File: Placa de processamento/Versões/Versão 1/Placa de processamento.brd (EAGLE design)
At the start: 90.2 x 100 mm, 12 parts

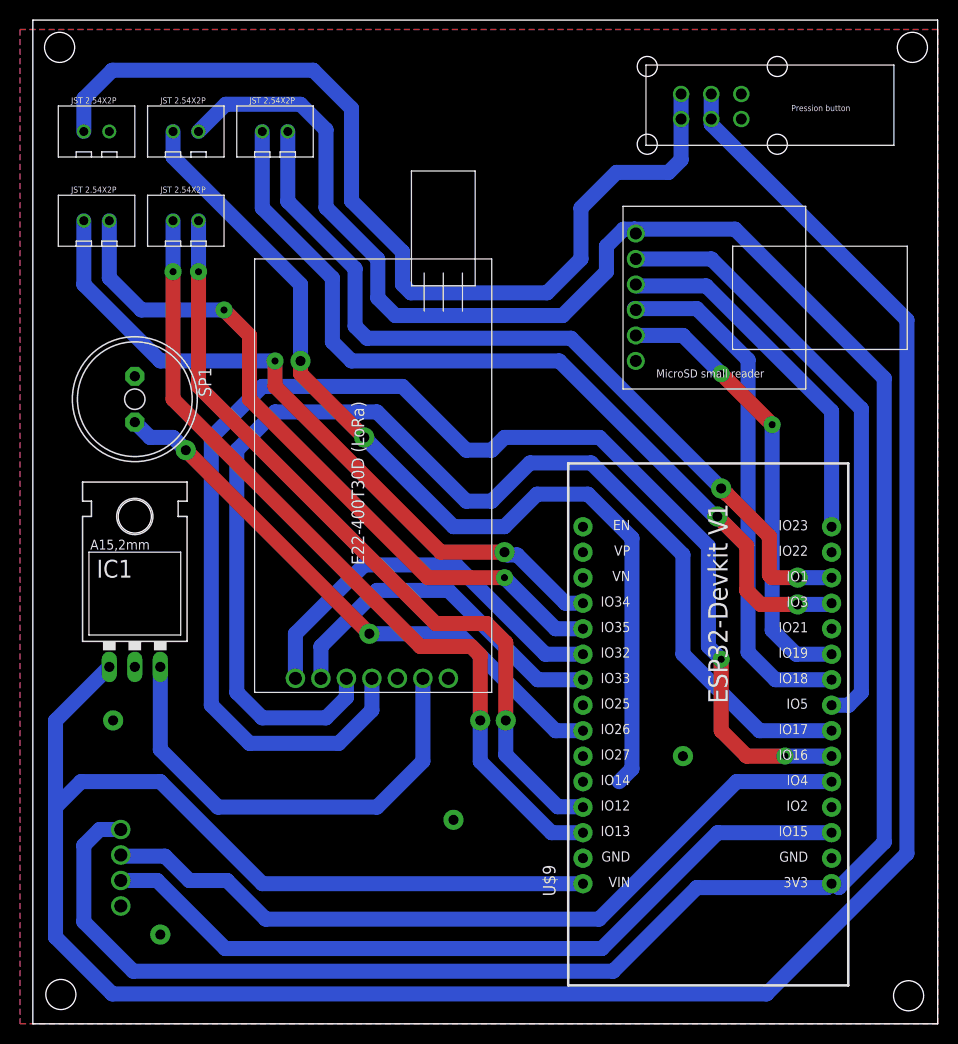
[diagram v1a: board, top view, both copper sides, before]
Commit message: FIX: consertando chave de acionamento
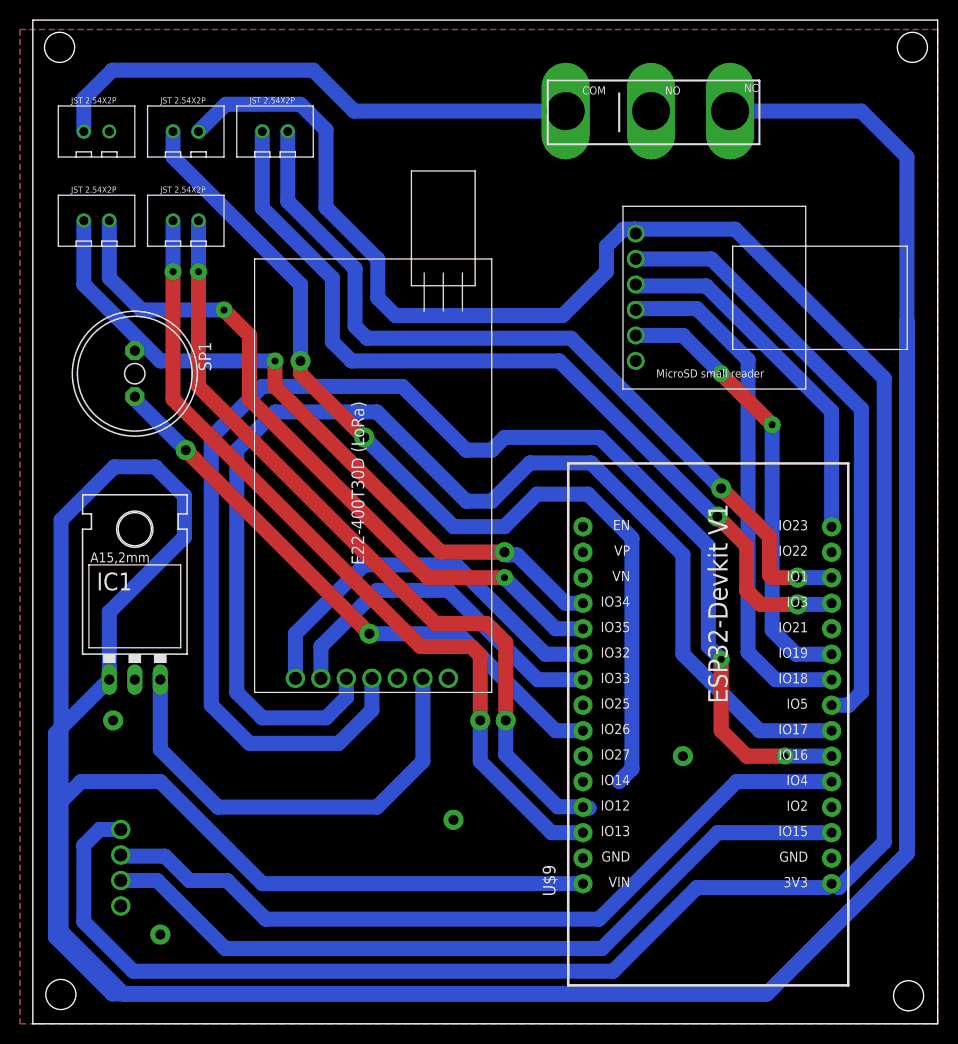
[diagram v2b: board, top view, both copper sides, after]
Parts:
- removed U$1: PRESSION_BUTTON, CRD:PRESSION_BUTTON_FOOTPRINT
- added U$11: CHAVE_SS-5GL, CRD:CHAVESS-5GL
- moved SP1 2.54 mm to (10.2, 64.8)
- moved IC1 1.27 mm to (10.2, 38.1)
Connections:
- net VIN: now also U$11.P$3; no longer U$1.PL2, U$1.PR2
- net V_BATTERY: now also U$11.P$1; no longer U$1.PL1, U$1.PR1
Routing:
- net VIN: track 263.7 -> 491.4 mm
- net V_BATTERY: track 95.5 -> 54.1 mm
- net 5V: track 46.9 -> 45.6 mm
- net SKIB2: track 78.7 -> 79.9 mm
- net BUZZER: track 57.4 -> 58.6 mm

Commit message: atualização placas
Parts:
- moved U$5 59.7 mm to (74.9, 91.4)
- moved U$3 50.9 mm to (57.1, 91.4)
- moved U$11 47.0 mm to (15.2, 88.9)
- moved U$10 42.0 mm to (66.0, 91.4)
- moved U$4 2.84 mm to (16.5, 77.5)
- moved U$6 2.84 mm to (7.62, 77.5)
- moved IC1 2.69 mm to (7.49, 38.5)
- moved U$7 2.54 mm to (25.3, 13.2)
- moved U$8 2.54 mm to (38.1, 50.8)
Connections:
- net 5V: now also U$9.30
- net VIN: no longer U$9.30
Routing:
- net VIN: track 491.4 -> 82.0 mm
- net SIGNAL1: track 96.7 -> 0.00 mm, vias 2 -> 0
- net OPTOACOPLADOR2: track 71.1 -> 0.00 mm, vias 2 -> 0
- net OPTOACOPLADOR1: track 70.7 -> 0.00 mm, vias 2 -> 0
- net 3V3: track 242.1 -> 194.6 mm
- net 5V: track 45.6 -> 71.5 mm
- net BUZZER: track 58.6 -> 78.8 mm
- net GND: track 0.00 -> 12.7 mm, vias 4 -> 2
- net SKIB1: track 82.7 -> 94.4 mm
- net SKIB2: track 79.9 -> 90.3 mm
- net RX0: track 87.1 -> 80.0 mm
- net TX0: track 82.3 -> 76.2 mm
- net TX2: track 121.8 -> 117.5 mm
- net RX2: track 139.0 -> 135.0 mm
- net MISO: track 44.7 -> 48.4 mm
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- removed copper zone on layer 1, net GND

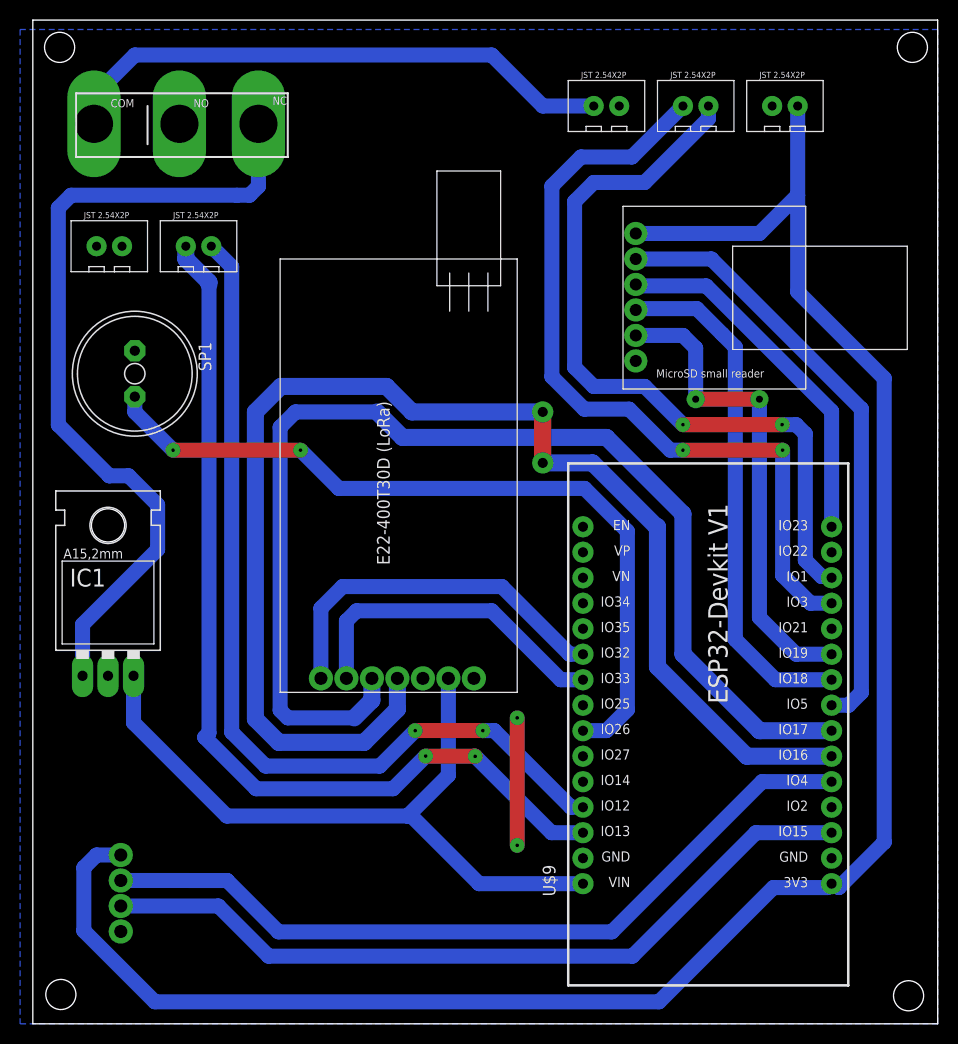
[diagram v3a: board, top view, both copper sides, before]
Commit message: CHORE: adicionando pads ovais na placa de processamento
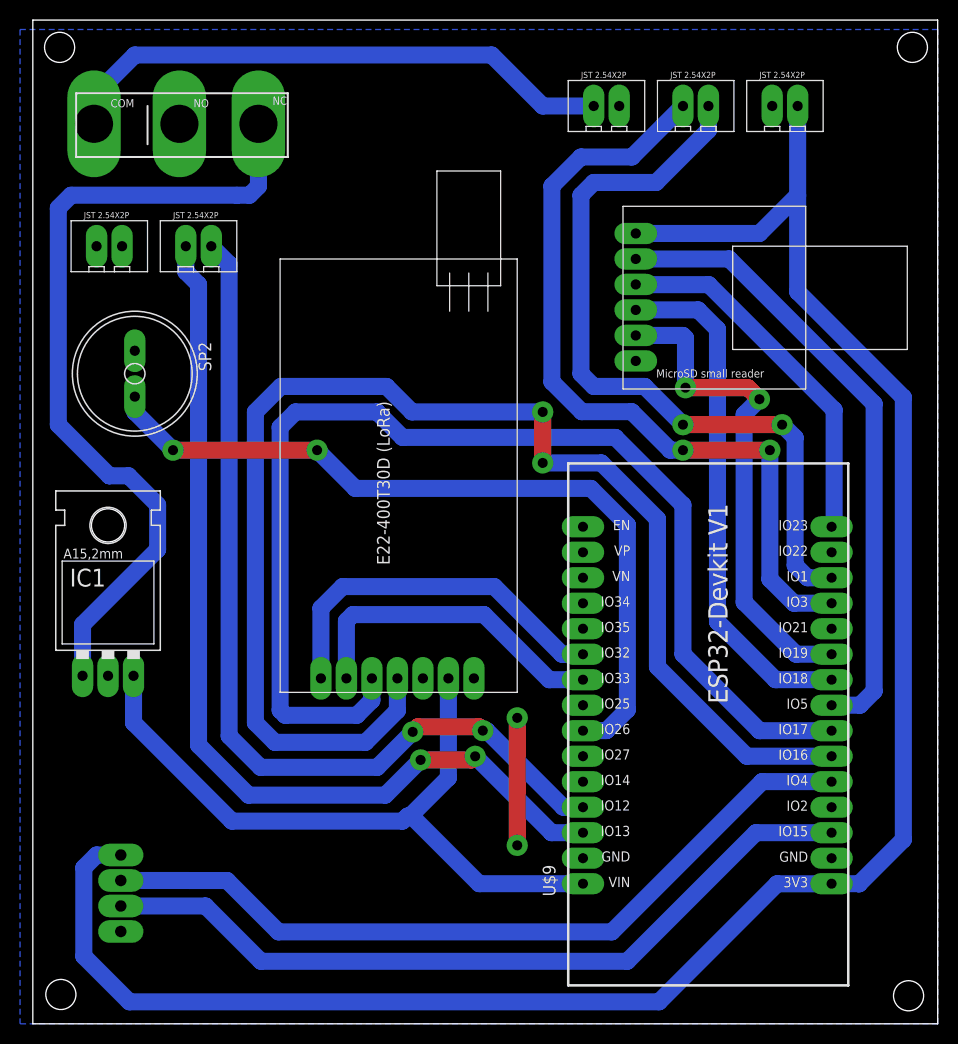
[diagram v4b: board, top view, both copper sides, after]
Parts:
- renumbered SP1 to SP2
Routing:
- net 3V3: track 194.6 -> 198.4 mm
- net CS: track 60.4 -> 63.2 mm
- net MISO: track 48.4 -> 49.6 mm
- net SKIB1: track 94.4 -> 95.4 mm
- net SKIB2: track 90.3 -> 91.1 mm
- net RX2: track 135.0 -> 135.8 mm
- net RX0: track 80.0 -> 80.6 mm

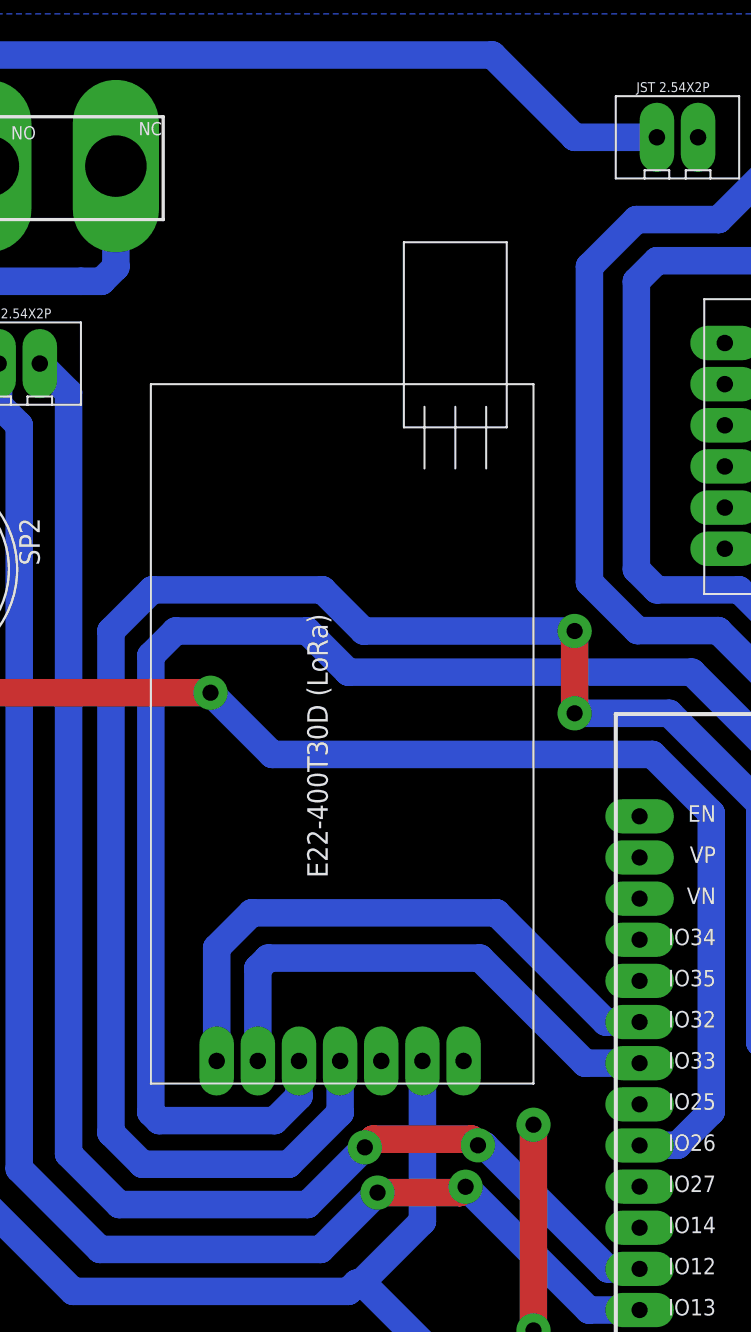
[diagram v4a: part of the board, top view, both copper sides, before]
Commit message: FIX: movendo LoRa para melhor posição
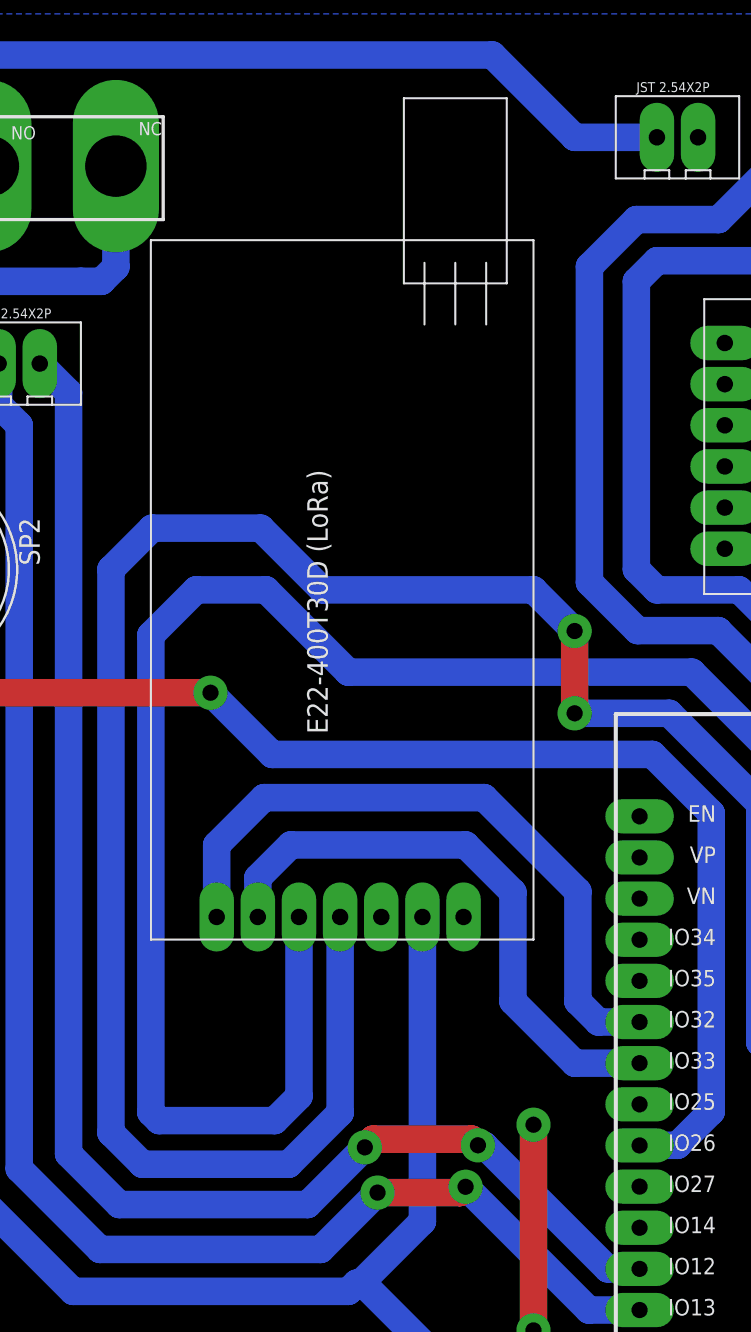
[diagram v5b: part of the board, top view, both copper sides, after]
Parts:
- moved U$8 8.89 mm to (38.1, 59.7)
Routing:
- net RX2: track 135.8 -> 150.1 mm
- net TX2: track 117.8 -> 129.5 mm
- net 5V: track 71.8 -> 80.7 mm
- net M0: track 36.8 -> 41.5 mm
- net M1: track 32.2 -> 36.3 mm
